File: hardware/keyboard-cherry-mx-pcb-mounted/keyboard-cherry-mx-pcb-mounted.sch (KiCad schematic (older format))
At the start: 15 parts, among them J2 SWDConn, SW1 RST, U1 STM32F413RHTx, Y1 8MHz

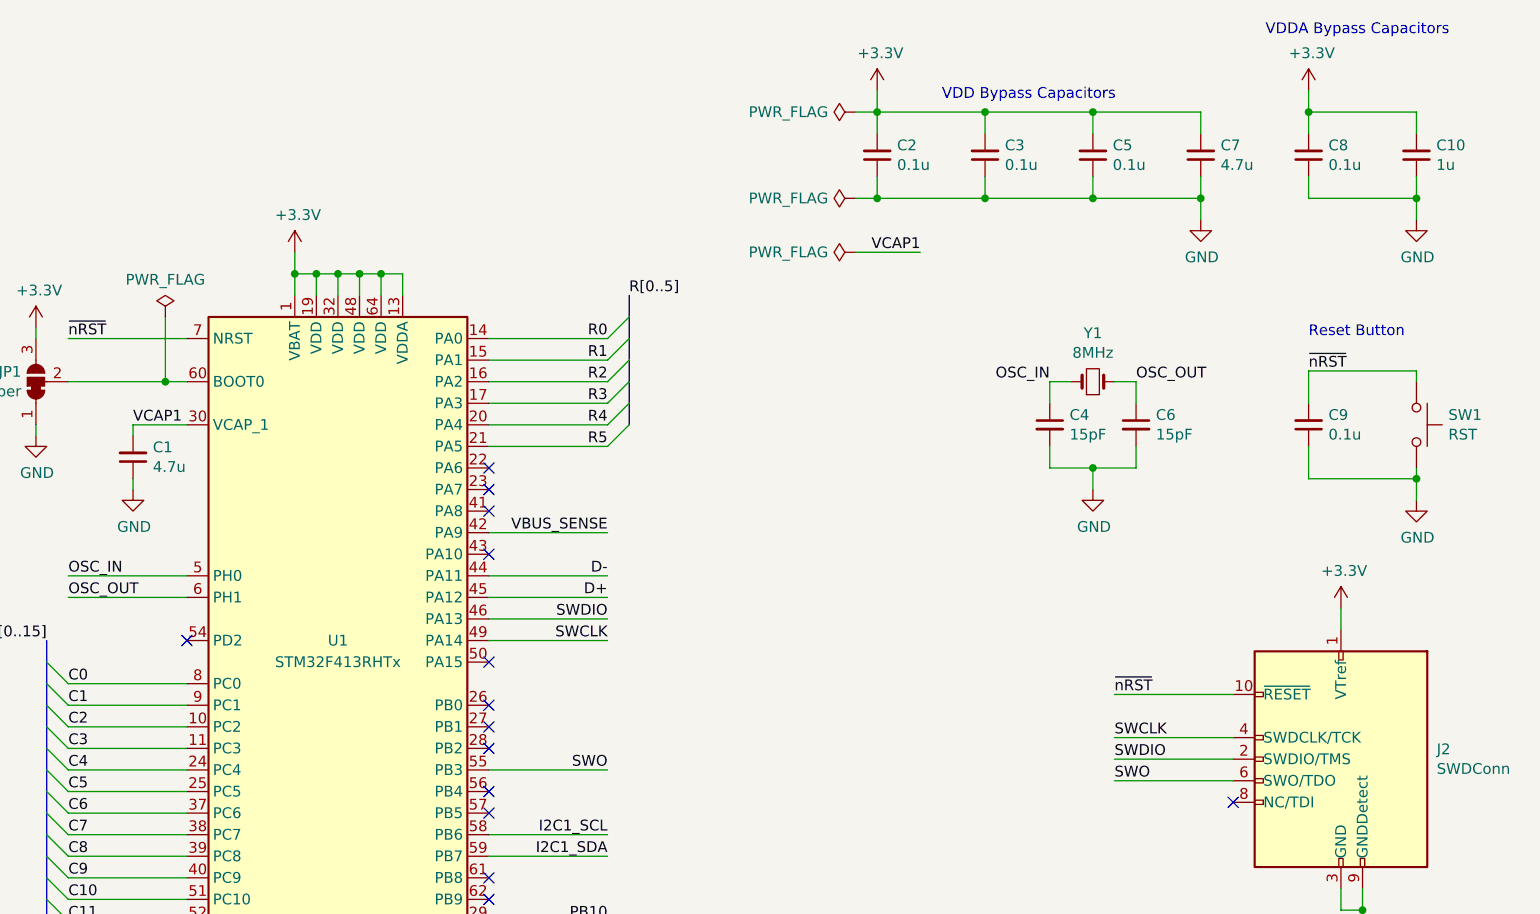
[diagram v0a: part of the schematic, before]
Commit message: Aligns the keys so the column connections are more consistent. e.g. right most keys will have same column connection.
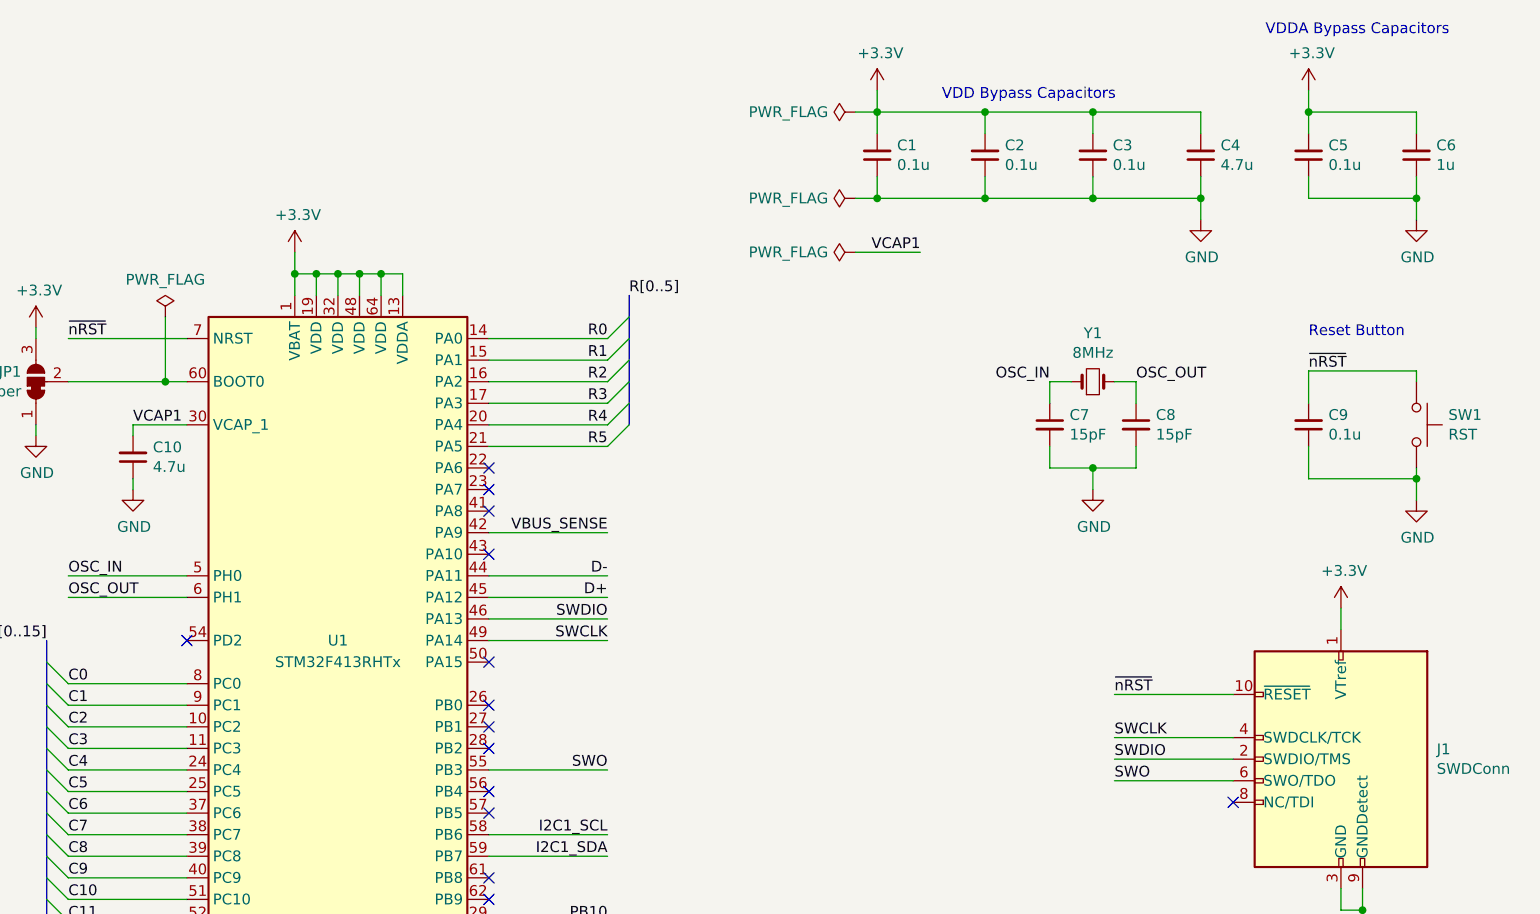
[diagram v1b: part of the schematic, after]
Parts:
- renumbered C2 to C1, C1 to C10, C3 to C2, C5 to C3, C7 to C4, C8 to C5, C10 to C6, C4 to C7, C6 to C8, J2 to J1
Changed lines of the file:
@@
 $EndComp
 $Comp
-L Device:C_Small C6
+L Device:C_Small C8
 U 1 1 5E7214AF
 P 9450 2750
-F 0 "C6" H 9542 2796 50  0000 L CNN
+F 0 "C8" H 9542 2796 50  0000 L CNN
 F 1 "15pF" H 9542 2705 50  0000 L CNN
 F 2 "Capacitor_SMD:C_0805_2012Metric" H 9450 2750 50  0001 C CNN
@@
 $EndComp
 $Comp
-L Device:C_Small C4
+L Device:C_Small C7
 U 1 1 5E722098
 P 9050 2750
-F 0 "C4" H 9142 2796 50  0000 L CNN
+F 0 "C7" H 9142 2796 50  0000 L CNN
 F 1 "15pF" H 9142 2705 50  0000 L CNN
 F 2 "Capacitor_SMD:C_0805_2012Metric" H 9050 2750 50  0001 C CNN
@@
 $EndComp
 $Comp
-L Device:C_Small C3
+L Device:C_Small C2
 U 1 1 5E73F523
 P 8750 1500
-F 0 "C3" H 8658 1454 50  0000 R CNN
+F 0 "C2" H 8658 1454 50  0000 R CNN
 F 1 "0.1u" H 8658 1545 50  0000 R CNN
 F 2 "Capacitor_SMD:C_0805_2012Metric" H 8750 1500 50  0001 C CNN
@@
 $EndComp
 $Comp
-L Device:C_Small C5
+L Device:C_Small C3
 U 1 1 5E73FD52
 P 9250 1500
-F 0 "C5" H 9158 1454 50  0000 R CNN
+F 0 "C3" H 9158 1454 50  0000 R CNN
 F 1 "0.1u" H 9158 1545 50  0000 R CNN
 F 2 "Capacitor_SMD:C_0805_2012Metric" H 9250 1500 50  0001 C CNN
@@
 $EndComp
 $Comp
-L Device:C_Small C7
+L Device:C_Small C4
 U 1 1 5E73FF6A
 P 9750 1500
-F 0 "C7" H 9658 1454 50  0000 R CNN
+F 0 "C4" H 9658 1454 50  0000 R CNN
 F 1 "4.7u" H 9658 1545 50  0000 R CNN
 F 2 "Capacitor_SMD:C_0805_2012Metric" H 9750 1500 50  0001 C CNN
@@
 $EndComp
 $Comp
-L Device:C_Small C8
+L Device:C_Small C5
 U 1 1 5E7436DF
 P 10250 1500
-F 0 "C8" H 10158 1454 50  0000 R CNN
+F 0 "C5" H 10158 1454 50  0000 R CNN
 F 1 "0.1u" H 10158 1545 50  0000 R CNN
 F 2 "Capacitor_SMD:C_0805_2012Metric" H 10250 1500 50  0001 C CNN
@@
 	8750 1300 9250 1300
 $Comp
-L power:GND #PWR08
+L power:GND #PWR03
 U 1 1 5E748424
 P 9750 1800
-F 0 "#PWR08" H 9750 1550 50  0001 C CNN
+F 0 "#PWR03" H 9750 1550 50  0001 C CNN
 F 1 "GND" H 9755 1627 50  0000 C CNN
 F 2 "" H 9750 1800 50  0001 C CNN
@@
 	9250 1700 8750 1700
 $Comp
-L Device:C_Small C10
+L Device:C_Small C6
 U 1 1 5E75FD02
 P 10750 1500
-F 0 "C10" H 10658 1454 50  0000 R CNN
+F 0 "C6" H 10658 1454 50  0000 R CNN
 F 1 "1u" H 10658 1545 50  0000 R CNN
 F 2 "Capacitor_SMD:C_0805_2012Metric" H 10750 1500 50  0001 C CNN
@@
 $EndComp
 $Comp
-L power:+3.3V #PWR09
+L power:+3.3V #PWR02
 U 1 1 5E760327
 P 10250 1200
-F 0 "#PWR09" H 10250 1050 50  0001 C CNN
+F 0 "#PWR02" H 10250 1050 50  0001 C CNN
 F 1 "+3.3V" H 10265 1373 50  0000 C CNN
 F 2 "" H 10250 1200 50  0001 C CNN
@@
 	10250 1300 10250 1400
 $Comp
-L power:GND #PWR010
+L power:GND #PWR04
 U 1 1 5E7639CA
 P 10750 1800
-F 0 "#PWR010" H 10750 1550 50  0001 C CNN
+F 0 "#PWR04" H 10750 1550 50  0001 C CNN
 F 1 "GND" H 10755 1627 50  0000 C CNN
 F 2 "" H 10750 1800 50  0001 C CNN
@@
 	10250 3000 10250 2850
 $Comp
-L power:GND #PWR011
+L power:GND #PWR010
 U 1 1 5E77E3D6
 P 10750 3100
-F 0 "#PWR011" H 10750 2850 50  0001 C CNN
+F 0 "#PWR010" H 10750 2850 50  0001 C CNN
 F 1 "GND" H 10755 2927 50  0000 C CNN
 F 2 "" H 10750 3100 50  0001 C CNN
@@
 Reset Button
 $Comp
-L power:GND #PWR07
+L power:GND #PWR09
 U 1 1 5E7915B9
 P 9250 3050
-F 0 "#PWR07" H 9250 2800 50  0001 C CNN
+F 0 "#PWR09" H 9250 2800 50  0001 C CNN
 F 1 "GND" H 9255 2877 50  0000 C CNN
 F 2 "" H 9250 3050 50  0001 C CNN
@@
 	6450 4650 7000 4650
 $Comp
-L power:GND #PWR03
+L power:GND #PWR08
 U 1 1 5E90C3E8
 P 4800 3050
-F 0 "#PWR03" H 4800 2800 50  0001 C CNN
+F 0 "#PWR08" H 4800 2800 50  0001 C CNN
 F 1 "GND" H 4805 2877 50  0000 C CNN
 F 2 "" H 4800 3050 50  0001 C CNN
@@
 	4350 2300 4350 2350
 $Comp
-L power:+3.3V #PWR01
+L power:+3.3V #PWR06
 U 1 1 5E8F336A
 P 4350 2300
-F 0 "#PWR01" H 4350 2150 50  0001 C CNN
+F 0 "#PWR06" H 4350 2150 50  0001 C CNN
 F 1 "+3.3V" H 4365 2473 50  0000 C CNN
 F 2 "" H 4350 2300 50  0001 C CNN
@@
 	4350 2800 4350 2750
 $Comp
-L power:GND #PWR02
+L power:GND #PWR07
 U 1 1 5E8F3363
 P 4350 2800
-F 0 "#PWR02" H 4350 2550 50  0001 C CNN
+F 0 "#PWR07" H 4350 2550 50  0001 C CNN
 F 1 "GND" H 4355 2627 50  0000 C CNN
 F 2 "" H 4350 2800 50  0001 C CNN
@@
 	5750 5850 5750 5750
 $Comp
-L power:GND #PWR05
+L power:GND #PWR013
 U 1 1 5E8CAB51
 P 5750 5850
-F 0 "#PWR05" H 5750 5600 50  0001 C CNN
+F 0 "#PWR013" H 5750 5600 50  0001 C CNN
 F 1 "GND" H 5755 5677 50  0000 C CNN
 F 2 "" H 5750 5850 50  0001 C CNN
@@
 	5550 1950 5550 2050
 $Comp
-L power:+3.3V #PWR04
+L power:+3.3V #PWR05
 U 1 1 5E8B41FD
 P 5550 1950
-F 0 "#PWR04" H 5550 1800 50  0001 C CNN
+F 0 "#PWR05" H 5550 1800 50  0001 C CNN
 F 1 "+3.3V" H 5565 2123 50  0000 C CNN
 F 2 "" H 5550 1950 50  0001 C CNN
@@
 	4800 2800 4800 2750
 $Comp
-L Device:C_Small C1
+L Device:C_Small C10
 U 1 1 5E71757F
 P 4800 2900
-F 0 "C1" H 4708 2854 50  0000 R CNN
+F 0 "C10" H 4708 2854 50  0000 R CNN
 F 1 "4.7u" H 4708 2945 50  0000 R CNN
 F 2 "Capacitor_SMD:C_0805_2012Metric" H 4800 2900 50  0001 C CNN
@@
 	8250 1400 8250 1300
 $Comp
-L Device:C_Small C2
+L Device:C_Small C1
 U 1 1 5E8A3593
 P 8250 1500
-F 0 "C2" H 8158 1454 50  0000 R CNN
+F 0 "C1" H 8158 1454 50  0000 R CNN
 F 1 "0.1u" H 8158 1545 50  0000 R CNN
 F 2 "Capacitor_SMD:C_0805_2012Metric" H 8250 1500 50  0001 C CNN
@@
 VDD Bypass Capacitors
 $Comp
-L power:+3.3V #PWR06
+L power:+3.3V #PWR01
 U 1 1 5E743BF3
 P 8250 1200
-F 0 "#PWR06" H 8250 1050 50  0001 C CNN
+F 0 "#PWR01" H 8250 1050 50  0001 C CNN
 F 1 "+3.3V" H 8265 1373 50  0000 C CNN
 F 2 "" H 8250 1200 50  0001 C CNN
@@
 	2550 1550 2000 1550
 $Comp
-L Connector:Conn_ARM_JTAG_SWD_10 J2
+L Connector:Conn_ARM_JTAG_SWD_10 J1
 U 1 1 5EA6CCCF
 P 10400 4300
-F 0 "J2" H 9956 4346 50  0000 R CNN
+F 0 "J1" H 9956 4346 50  0000 R CNN
 F 1 "SWDConn" H 9956 4255 50  0000 R CNN
 F 2 "Connector:Tag-Connect_TC2050-IDC-NL_2x05_P1.27mm_Vertical" H 10400 4300 50  0001 C CNN
@@
 $EndComp
 $Comp
-L power:GND #PWR0104
+L power:GND #PWR012
 U 1 1 5EA7066F
 P 10500 5100
-F 0 "#PWR0104" H 10500 4850 50  0001 C CNN
+F 0 "#PWR012" H 10500 4850 50  0001 C CNN
 F 1 "GND" H 10505 4927 50  0000 C CNN
 F 2 "" H 10500 5100 50  0001 C CNN
@@
 	9900 4200 9350 4200
 $Comp
-L power:+3.3V #PWR0105
+L power:+3.3V #PWR011
 U 1 1 5EAB5F0F
 P 10400 3600
-F 0 "#PWR0105" H 10400 3450 50  0001 C CNN
+F 0 "#PWR011" H 10400 3450 50  0001 C CNN
 F 1 "+3.3V" H 10415 3773 50  0000 C CNN
 F 2 "" H 10400 3600 50  0001 C CNN
@@
 	9350 4000 9900 4000
 $Comp
-L power:PWR_FLAG #FLG01
+L power:PWR_FLAG #FLG02
 U 1 1 5EAC43B9
 P 8150 1700
-F 0 "#FLG01" H 8150 1775 50  0001 C CNN
+F 0 "#FLG02" H 8150 1775 50  0001 C CNN
 F 1 "PWR_FLAG" V 8150 1827 50  0000 L CNN
 F 2 "" H 8150 1700 50  0001 C CNN
@@
 VCAP1
 $Comp
-L power:PWR_FLAG #FLG0103
+L power:PWR_FLAG #FLG03
 U 1 1 5EB0BDAA
 P 8150 1950
-F 0 "#FLG0103" H 8150 2025 50  0001 C CNN
+F 0 "#FLG03" H 8150 2025 50  0001 C CNN
 F 1 "PWR_FLAG" V 8150 2077 50  0000 L CNN
 F 2 "" H 8150 1950 50  0001 C CNN
@@
 Connection ~ 5550 2050
 $Comp
-L power:PWR_FLAG #FLG0102
+L power:PWR_FLAG #FLG04
 U 1 1 5EB62660
 P 4950 2250
-F 0 "#FLG0102" H 4950 2325 50  0001 C CNN
+F 0 "#FLG04" H 4950 2325 50  0001 C CNN
 F 1 "PWR_FLAG" H 4950 2423 50  0000 C CNN
 F 2 "" H 4950 2250 50  0001 C CNN
@@
 	4950 2550 4500 2550
 $Comp
-L power:PWR_FLAG #FLG0104
+L power:PWR_FLAG #FLG01
 U 1 1 5E7192AF
 P 8150 1300
-F 0 "#FLG0104" H 8150 1375 50  0001 C CNN
+F 0 "#FLG01" H 8150 1375 50  0001 C CNN
 F 1 "PWR_FLAG" V 8150 1427 50  0000 L CNN
 F 2 "" H 8150 1300 50  0001 C CNN

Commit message: Changes bypass capacitors for the stm32f413 to 0603 on the cherry mx pcb mounted keyboard. Also the sensors were not centered in between row 0 and 1 so that was fixed. Y position not 2.6375in
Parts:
- C1, C10, C2, C3, C4, C5, C6, C7, C8: footprint Capacitor_SMD:C_0805_2012Metric -> Capacitor_SMD:C_0603_1608Metric
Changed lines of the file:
@@
 F 0 "C8" H 9542 2796 50  0000 L CNN
 F 1 "15pF" H 9542 2705 50  0000 L CNN
-F 2 "Capacitor_SMD:C_0805_2012Metric" H 9450 2750 50  0001 C CNN
+F 2 "Capacitor_SMD:C_0603_1608Metric" H 9450 2750 50  0001 C CNN
 F 3 "~" H 9450 2750 50  0001 C CNN
 	1    9450 2750
@@
 F 0 "C7" H 9142 2796 50  0000 L CNN
 F 1 "15pF" H 9142 2705 50  0000 L CNN
-F 2 "Capacitor_SMD:C_0805_2012Metric" H 9050 2750 50  0001 C CNN
+F 2 "Capacitor_SMD:C_0603_1608Metric" H 9050 2750 50  0001 C CNN
 F 3 "~" H 9050 2750 50  0001 C CNN
 	1    9050 2750
@@
 F 0 "C2" H 8658 1454 50  0000 R CNN
 F 1 "0.1u" H 8658 1545 50  0000 R CNN
-F 2 "Capacitor_SMD:C_0805_2012Metric" H 8750 1500 50  0001 C CNN
+F 2 "Capacitor_SMD:C_0603_1608Metric" H 8750 1500 50  0001 C CNN
 F 3 "~" H 8750 1500 50  0001 C CNN
 	1    8750 1500
@@
 F 0 "C3" H 9158 1454 50  0000 R CNN
 F 1 "0.1u" H 9158 1545 50  0000 R CNN
-F 2 "Capacitor_SMD:C_0805_2012Metric" H 9250 1500 50  0001 C CNN
+F 2 "Capacitor_SMD:C_0603_1608Metric" H 9250 1500 50  0001 C CNN
 F 3 "~" H 9250 1500 50  0001 C CNN
 	1    9250 1500
@@
 F 0 "C4" H 9658 1454 50  0000 R CNN
 F 1 "4.7u" H 9658 1545 50  0000 R CNN
-F 2 "Capacitor_SMD:C_0805_2012Metric" H 9750 1500 50  0001 C CNN
+F 2 "Capacitor_SMD:C_0603_1608Metric" H 9750 1500 50  0001 C CNN
 F 3 "~" H 9750 1500 50  0001 C CNN
 	1    9750 1500
@@
 F 0 "C5" H 10158 1454 50  0000 R CNN
 F 1 "0.1u" H 10158 1545 50  0000 R CNN
-F 2 "Capacitor_SMD:C_0805_2012Metric" H 10250 1500 50  0001 C CNN
+F 2 "Capacitor_SMD:C_0603_1608Metric" H 10250 1500 50  0001 C CNN
 F 3 "~" H 10250 1500 50  0001 C CNN
 	1    10250 1500
@@
 F 0 "C6" H 10658 1454 50  0000 R CNN
 F 1 "1u" H 10658 1545 50  0000 R CNN
-F 2 "Capacitor_SMD:C_0805_2012Metric" H 10750 1500 50  0001 C CNN
+F 2 "Capacitor_SMD:C_0603_1608Metric" H 10750 1500 50  0001 C CNN
 F 3 "~" H 10750 1500 50  0001 C CNN
 	1    10750 1500
@@
 F 0 "C10" H 4708 2854 50  0000 R CNN
 F 1 "4.7u" H 4708 2945 50  0000 R CNN
-F 2 "Capacitor_SMD:C_0805_2012Metric" H 4800 2900 50  0001 C CNN
+F 2 "Capacitor_SMD:C_0603_1608Metric" H 4800 2900 50  0001 C CNN
 F 3 "~" H 4800 2900 50  0001 C CNN
 	1    4800 2900
@@
 F 0 "C1" H 8158 1454 50  0000 R CNN
 F 1 "0.1u" H 8158 1545 50  0000 R CNN
-F 2 "Capacitor_SMD:C_0805_2012Metric" H 8250 1500 50  0001 C CNN
+F 2 "Capacitor_SMD:C_0603_1608Metric" H 8250 1500 50  0001 C CNN
 F 3 "~" H 8250 1500 50  0001 C CNN
 	1    8250 1500

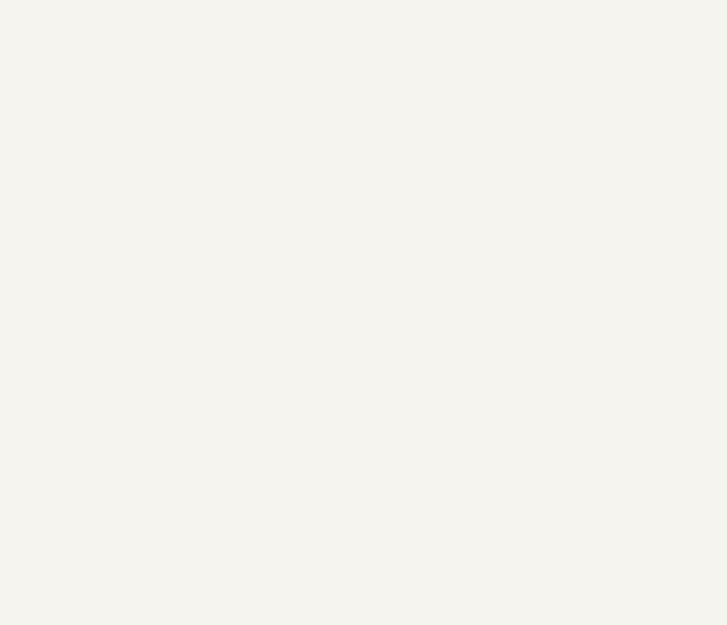
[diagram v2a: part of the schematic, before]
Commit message: Adds mounting holes to the cherry mx pcb mounted keyboard.
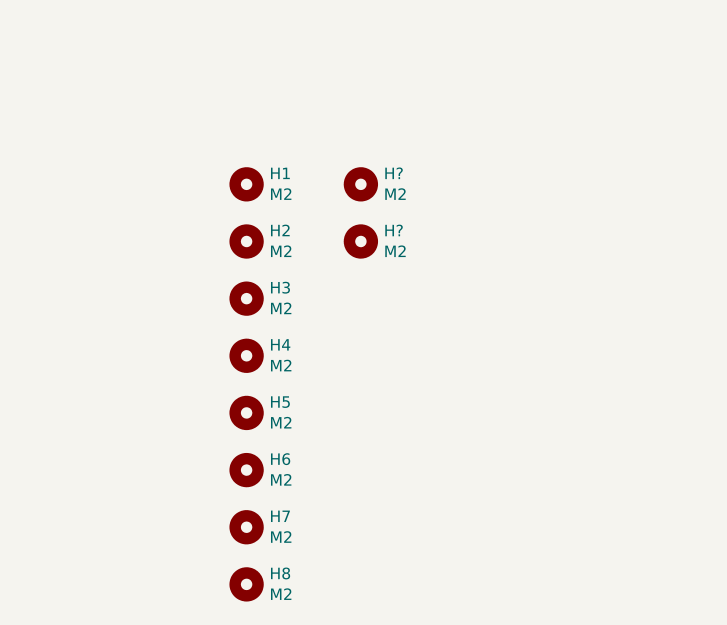
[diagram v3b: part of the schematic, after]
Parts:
- added H1, H2, H3, H4, H5, H6, H7, H8, H? (x2): M2, MountingHole:MountingHole_2.2mm_M2, symbol Mechanical:MountingHole
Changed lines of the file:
@@
 Wire Wire Line
 	2550 3000 2000 3000
+$Comp
+L Mechanical:MountingHole H1
+U 1 1 5E749BAA
+P 2000 5500
+F 0 "H1" H 2100 5546 50  0000 L CNN
+F 1 "M2" H 2100 5455 50  0000 L CNN
+F 2 "MountingHole:MountingHole_2.2mm_M2" H 2000 5500 50  0001 C CNN
+F 3 "~" H 2000 5500 50  0001 C CNN
+	1    2000 5500
+	1    0    0    -1
+$EndComp
+$Comp
+L Mechanical:MountingHole H2
+U 1 1 5E74A79D
+P 2000 5750
+F 0 "H2" H 2100 5796 50  0000 L CNN
+F 1 "M2" H 2100 5705 50  0000 L CNN
+F 2 "MountingHole:MountingHole_2.2mm_M2" H 2000 5750 50  0001 C CNN
+F 3 "~" H 2000 5750 50  0001 C CNN
+	1    2000 5750
+	1    0    0    -1
+$EndComp
+$Comp
+L Mechanical:MountingHole H3
+U 1 1 5E74AA5A
+P 2000 6000
+F 0 "H3" H 2100 6046 50  0000 L CNN
+F 1 "M2" H 2100 5955 50  0000 L CNN
+F 2 "MountingHole:MountingHole_2.2mm_M2" H 2000 6000 50  0001 C CNN
+F 3 "~" H 2000 6000 50  0001 C CNN
+	1    2000 6000
+	1    0    0    -1
+$EndComp
+$Comp
+L Mechanical:MountingHole H4
+U 1 1 5E74AC29
+P 2000 6250
+F 0 "H4" H 2100 6296 50  0000 L CNN
+F 1 "M2" H 2100 6205 50  0000 L CNN
+F 2 "MountingHole:MountingHole_2.2mm_M2" H 2000 6250 50  0001 C CNN
+F 3 "~" H 2000 6250 50  0001 C CNN
+	1    2000 6250
+	1    0    0    -1
+$EndComp
+$Comp
+L Mechanical:MountingHole H5
+U 1 1 5E74B1D4
+P 2000 6500
+F 0 "H5" H 2100 6546 50  0000 L CNN
+F 1 "M2" H 2100 6455 50  0000 L CNN
+F 2 "MountingHole:MountingHole_2.2mm_M2" H 2000 6500 50  0001 C CNN
+F 3 "~" H 2000 6500 50  0001 C CNN
+	1    2000 6500
+	1    0    0    -1
+$EndComp
+$Comp
+L Mechanical:MountingHole H6
+U 1 1 5E74DA72
+P 2000 6750
+F 0 "H6" H 2100 6796 50  0000 L CNN
+F 1 "M2" H 2100 6705 50  0000 L CNN
+F 2 "MountingHole:MountingHole_2.2mm_M2" H 2000 6750 50  0001 C CNN
+F 3 "~" H 2000 6750 50  0001 C CNN
+	1    2000 6750
+	1    0    0    -1
+$EndComp
+$Comp
+L Mechanical:MountingHole H7
+U 1 1 5E74DCCC
+P 2000 7000
+F 0 "H7" H 2100 7046 50  0000 L CNN
+F 1 "M2" H 2100 6955 50  0000 L CNN
+F 2 "MountingHole:MountingHole_2.2mm_M2" H 2000 7000 50  0001 C CNN
+F 3 "~" H 2000 7000 50  0001 C CNN
+	1    2000 7000
+	1    0    0    -1
+$EndComp
+$Comp
+L Mechanical:MountingHole H8
+U 1 1 5E74E871
+P 2000 7250
+F 0 "H8" H 2100 7296 50  0000 L CNN
+F 1 "M2" H 2100 7205 50  0000 L CNN
+F 2 "MountingHole:MountingHole_2.2mm_M2" H 2000 7250 50  0001 C CNN
+F 3 "~" H 2000 7250 50  0001 C CNN
+	1    2000 7250
+	1    0    0    -1
+$EndComp
+$Comp
+L Mechanical:MountingHole H?
+U 1 1 5E7549C0
+P 2500 5500
+F 0 "H?" H 2600 5546 50  0000 L CNN
+F 1 "M2" H 2600 5455 50  0000 L CNN
+F 2 "MountingHole:MountingHole_2.2mm_M2" H 2500 5500 50  0001 C CNN
+F 3 "~" H 2500 5500 50  0001 C CNN
+	1    2500 5500
+	1    0    0    -1
+$EndComp
+$Comp
+L Mechanical:MountingHole H?
+U 1 1 5E7549C6
+P 2500 5750
+F 0 "H?" H 2600 5796 50  0000 L CNN
+F 1 "M2" H 2600 5705 50  0000 L CNN
+F 2 "MountingHole:MountingHole_2.2mm_M2" H 2500 5750 50  0001 C CNN
+F 3 "~" H 2500 5750 50  0001 C CNN
+	1    2500 5750
+	1    0    0    -1
+$EndComp
 Wire Bus Line
 	7100 2150 7100 2750
